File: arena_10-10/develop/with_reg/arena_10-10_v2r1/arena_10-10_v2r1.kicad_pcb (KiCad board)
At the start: 6 copper layers, 248.9 x 228.6 mm, 538 parts, among them J1 Cetus RJ45 Magjack, J10 Conn_01x05, J100 PinSocket_1x24_P2.54mm_Vertic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, J101 PinSocket_1x24_P2.54mm_Vertic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, J102 PinSocket_2x03_P2.00mm_Vertic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, J11 Conn_01x05, J12 Conn_01x05, J13 Conn_01x05, J14 Conn_01x05, J15 Conn_01x05, J16 Conn_01x05, J17 Conn_01x05, J18 Conn_01x05, J19 Conn_01x05, J2 Conn_01x02, J20 Conn_01x05, J21 Conn_01x05, J22 Conn_01x05, J23 Conn_01x05, J24 Conn_01x05, J25 Barrel_Jack, J26 XT30 Female, J27 Conn_Coaxial, J28 Conn_Coaxial, J29 Conn_Coaxial, J3 Conn_Coaxial, J30 Conn_01x02, J4 Conn_Coaxial, J5 Conn_01x05, J6 Conn_01x05, J7 Conn_01x05, J8 Conn_01x05, J9 Conn_01x05, P1 NA, P10 NA, P2 NA, P3 NA, P4 NA, P5 NA, P6 NA, P7 NA, P8 NA, P9 NA, SW1 SW_SPDT, U1 Teensy4.1, U10 74LVC2G17, U100 74LVC1G125, U101 74LVC2G17, U102 SN74HCS08, U103 SN74HCS08, U104 74LVC1G125, U105 74LVC2G17, U106 SN74HCS08, U107 SN74HCS08, U108 74LVC1G125, U109 74LVC2G17, U11 74LVC2G17, U110 NID100-5, U112 74LVC1G125, U113 74LVC2G17, U116 74LVC1G125, U117 74LVC2G17, U12 74LVC2G17, U120 74LVC1G125, U121 74LVC2G17, U124 74LVC1G125, U125 74LVC2G17, U13 74LVC2G17, U14 74LVC2G17, U15 74LVC2G17, U16 74LVC2G17, U17 74LVC2G17, U18 74LVC2G17, U19 74LVC2G17, U2 SN74LVC1T45DBV, U20 74LVC2G17, U21 74LVC2G17, U22 74LVC2G17, U23 74LVC2G17, U24 74LVC2G17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

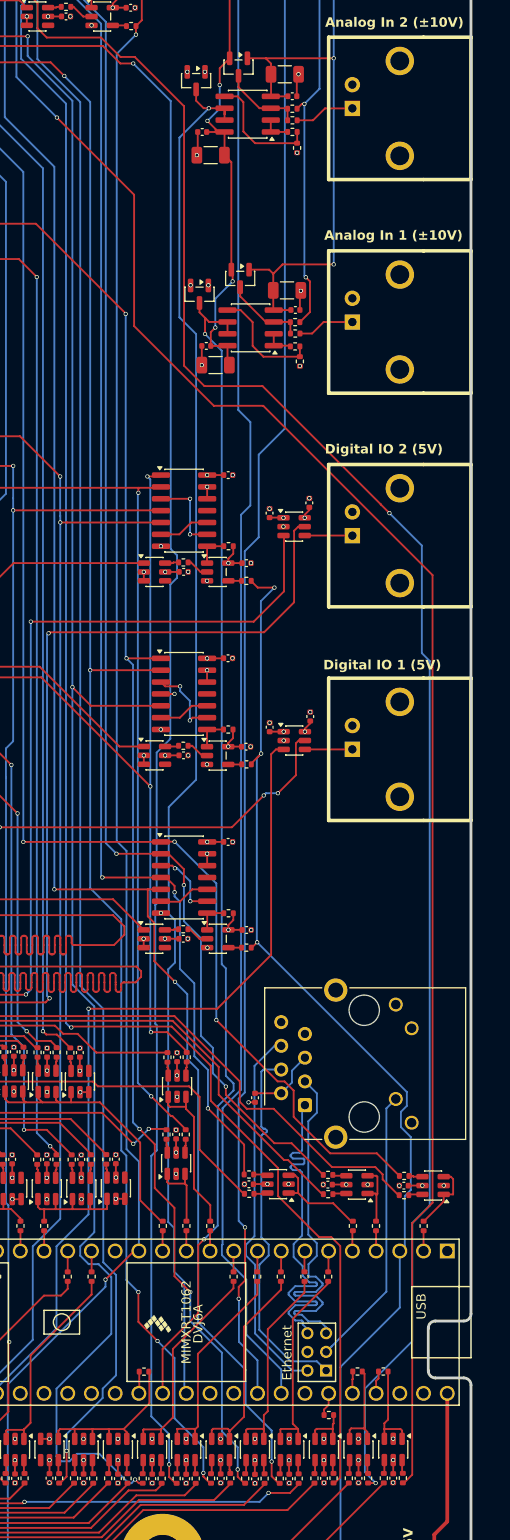
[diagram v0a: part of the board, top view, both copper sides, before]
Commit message: Added isolated island for analog subsystem.
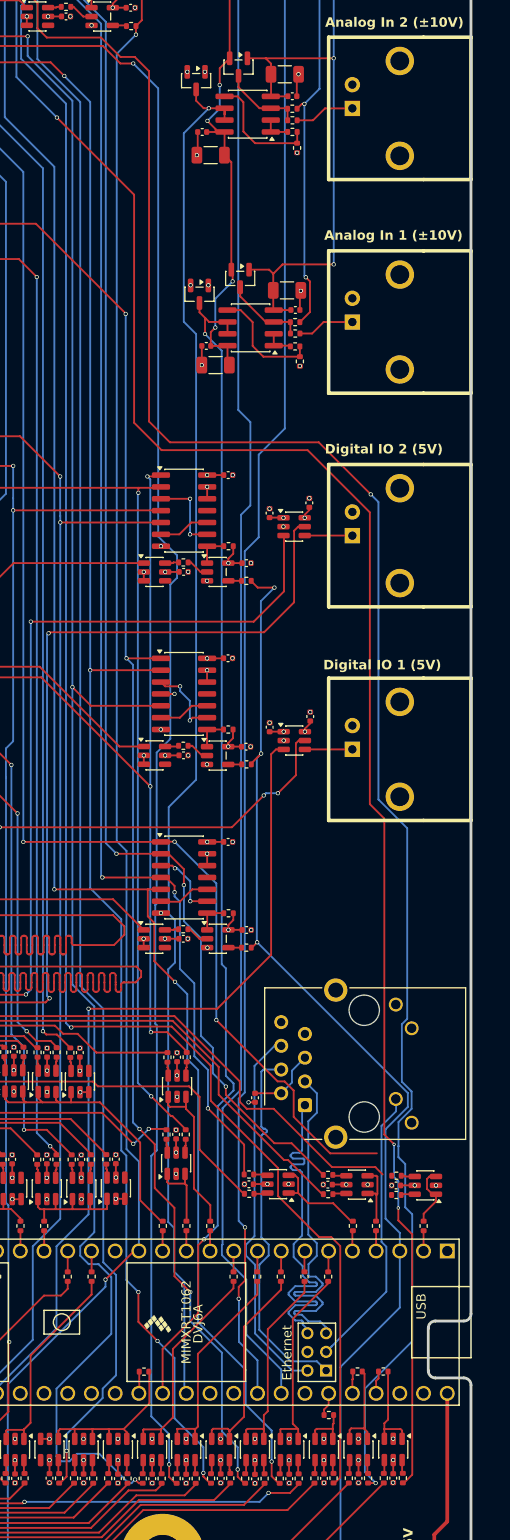
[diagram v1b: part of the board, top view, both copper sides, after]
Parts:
- moved C16 0.83 mm to (304.4, 239.7)
- moved R48 0.83 mm to (304.4, 240.8)
- moved R49 0.83 mm to (304.4, 238.7)
- moved U16 0.83 mm to (307.5, 239.7)
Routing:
- net /Fan Out/PAN.CS_18_P5: track 329.7 -> 335.5 mm
- net /Fan Out/PAN.CS_17_P5: track 320.8 -> 325.1 mm, vias 2 -> 4
- net /Fan Out/PAN.CS_00_P6: track 214.4 -> 211.0 mm
- net /Fan Out/PAN.CS_00_P1: track 203.2 -> 200.3 mm
- net /Fan Out/TNY.MISO_B1: track 226.8 -> 228.0 mm
- net /Fan Out/TNY.CS_00: track 7.56 -> 6.79 mm
